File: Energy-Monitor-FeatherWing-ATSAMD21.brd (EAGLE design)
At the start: 50.8 x 22.9 mm, 32 parts

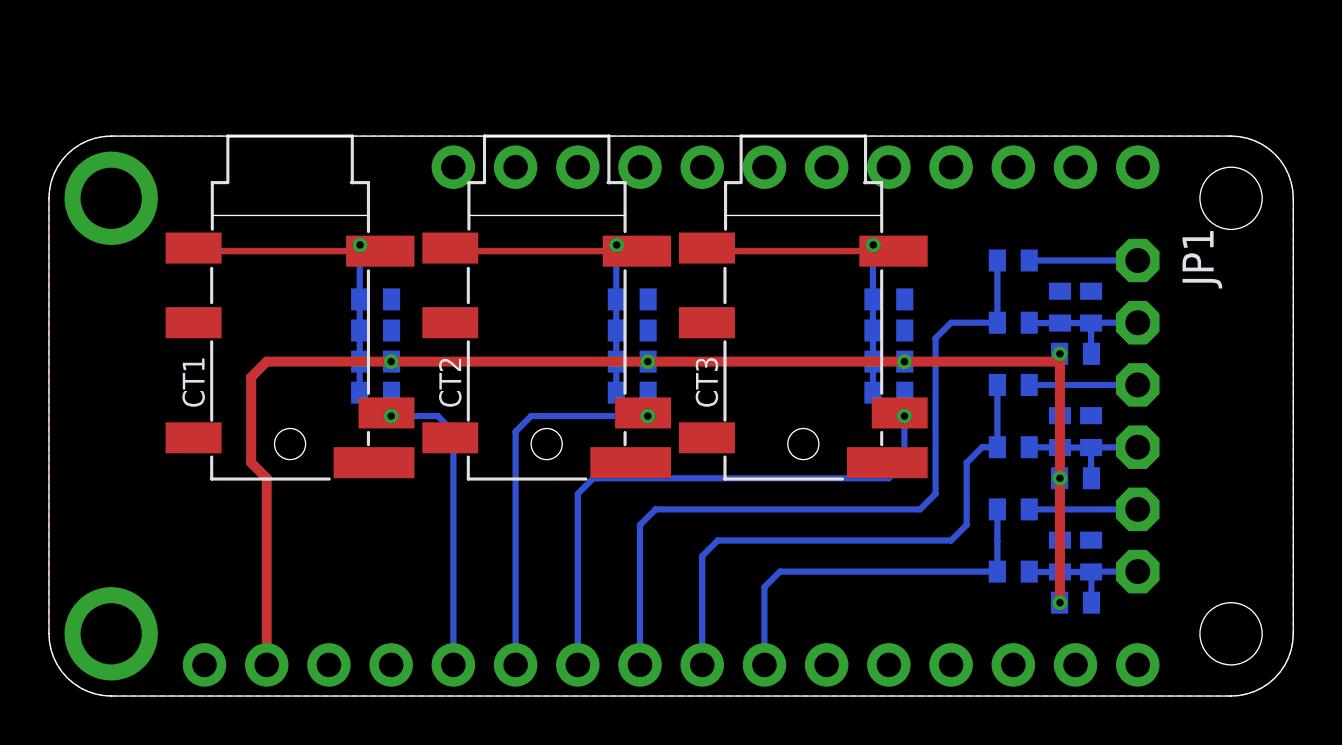
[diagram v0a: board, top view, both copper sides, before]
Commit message: Fix layout issues - the TRS jacks have a rim that is not flush with the PCB, had to sacrifice some FeatherWing pins.
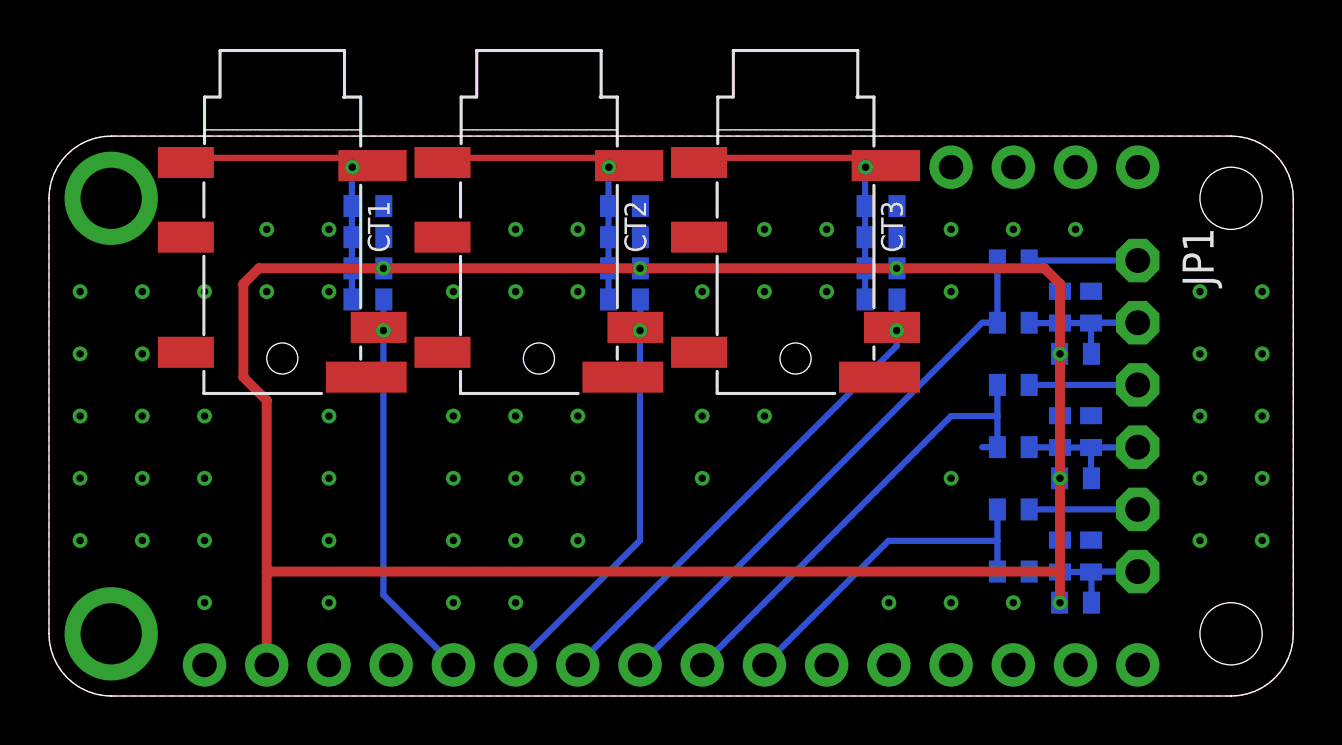
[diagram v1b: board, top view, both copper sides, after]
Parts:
- moved C3 3.82 mm to (34.0, 20.0)
- moved R7 3.82 mm to (34.0, 18.7)
- moved C1 3.82 mm to (13.0, 20.0)
- moved C2 3.82 mm to (23.5, 20.0)
- moved R1 3.82 mm to (13.0, 18.7)
- moved R4 3.82 mm to (23.5, 18.7)
- moved R8 3.82 mm to (34.0, 17.5)
- moved R9 3.82 mm to (34.0, 16.2)
- moved R2 3.82 mm to (13.0, 17.5)
- moved R3 3.82 mm to (13.0, 16.2)
- moved R5 3.82 mm to (23.5, 17.5)
- moved R6 3.82 mm to (23.5, 16.2)
- moved CT1 3.51 mm to (9.53, 18.7)
- moved CT2 3.51 mm to (20.0, 18.7)
- moved CT3 3.51 mm to (30.5, 18.7)
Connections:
- net N$6 renamed AC_GND
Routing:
- net VCC: track 55.5 -> 98.2 mm
- net N$5: track 30.0 -> 22.9 mm
- net N$3: track 24.0 -> 20.6 mm
- net N$8: track 22.4 -> 19.4 mm
- net N$1: track 13.6 -> 16.4 mm
- net CT1_REF: track 15.7 -> 13.7 mm
- net N$11: track 15.5 -> 14.1 mm
- net CT2_REF: track 14.7 -> 13.6 mm
- net N$2: track 16.4 -> 17.3 mm

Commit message: Better name silkscreen and more GND vias
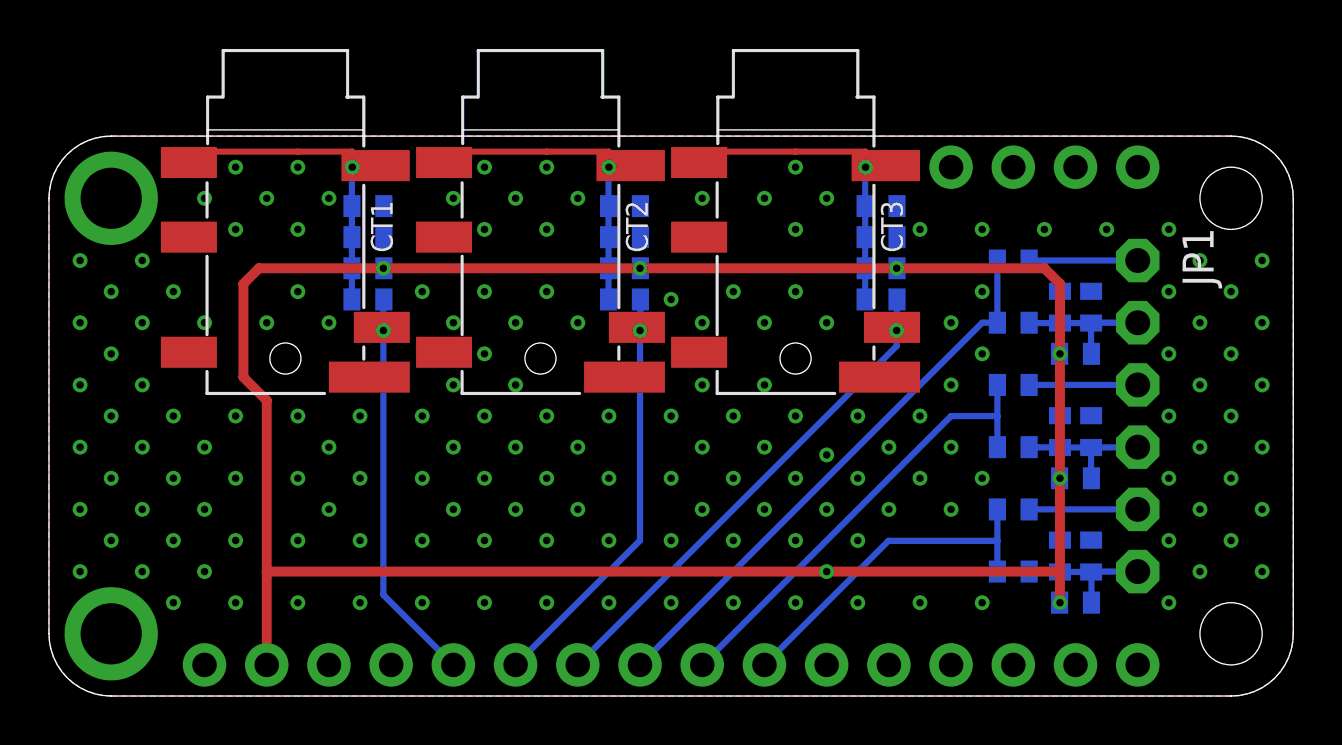
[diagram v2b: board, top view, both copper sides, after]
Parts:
- moved CT1 0.13 mm to (9.65, 18.7)
- moved CT2 0.06 mm to (20.1, 18.7)
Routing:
- net CT2_REF: track 13.6 -> 14.6 mm
- net CT3_REF: track 13.7 -> 14.3 mm
- net N$8: track 19.4 -> 18.8 mm
